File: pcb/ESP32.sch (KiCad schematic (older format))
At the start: 5 parts, among them U1 ESP32-WROOM

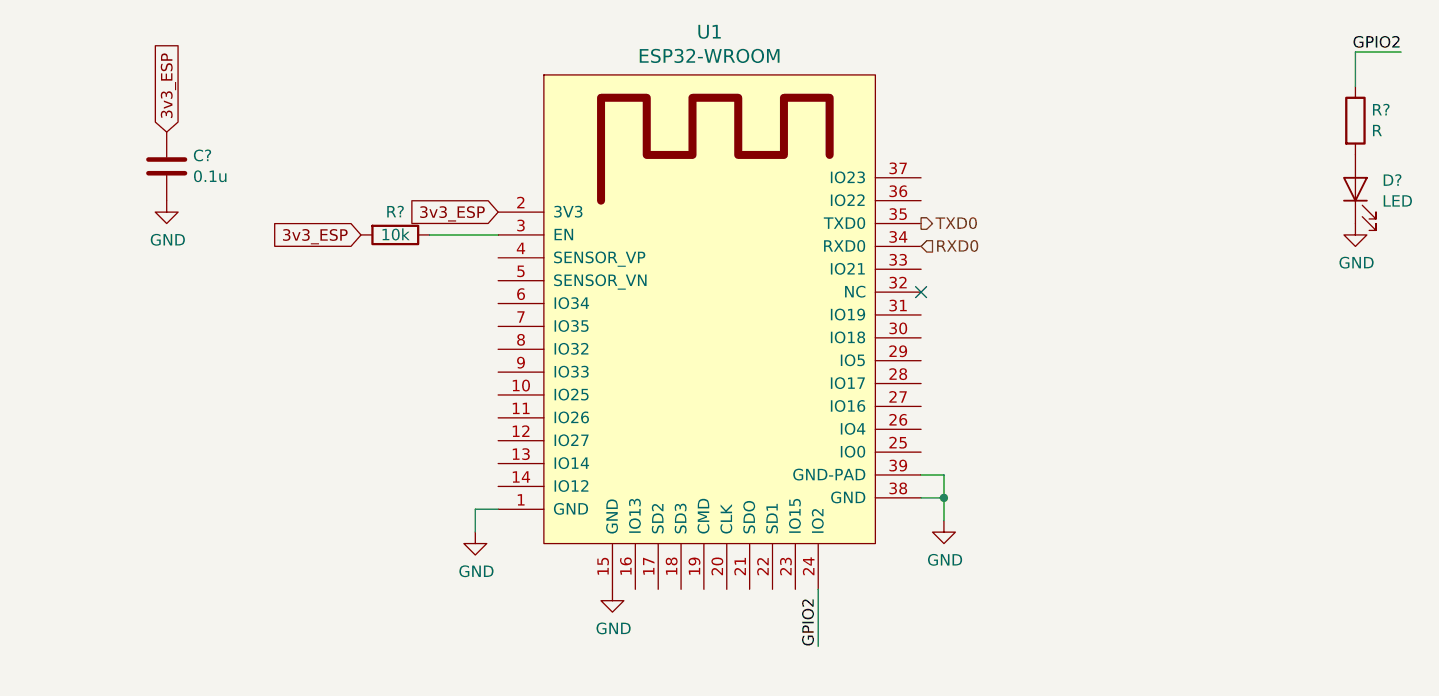
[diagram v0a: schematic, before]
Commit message: RTC to PCB
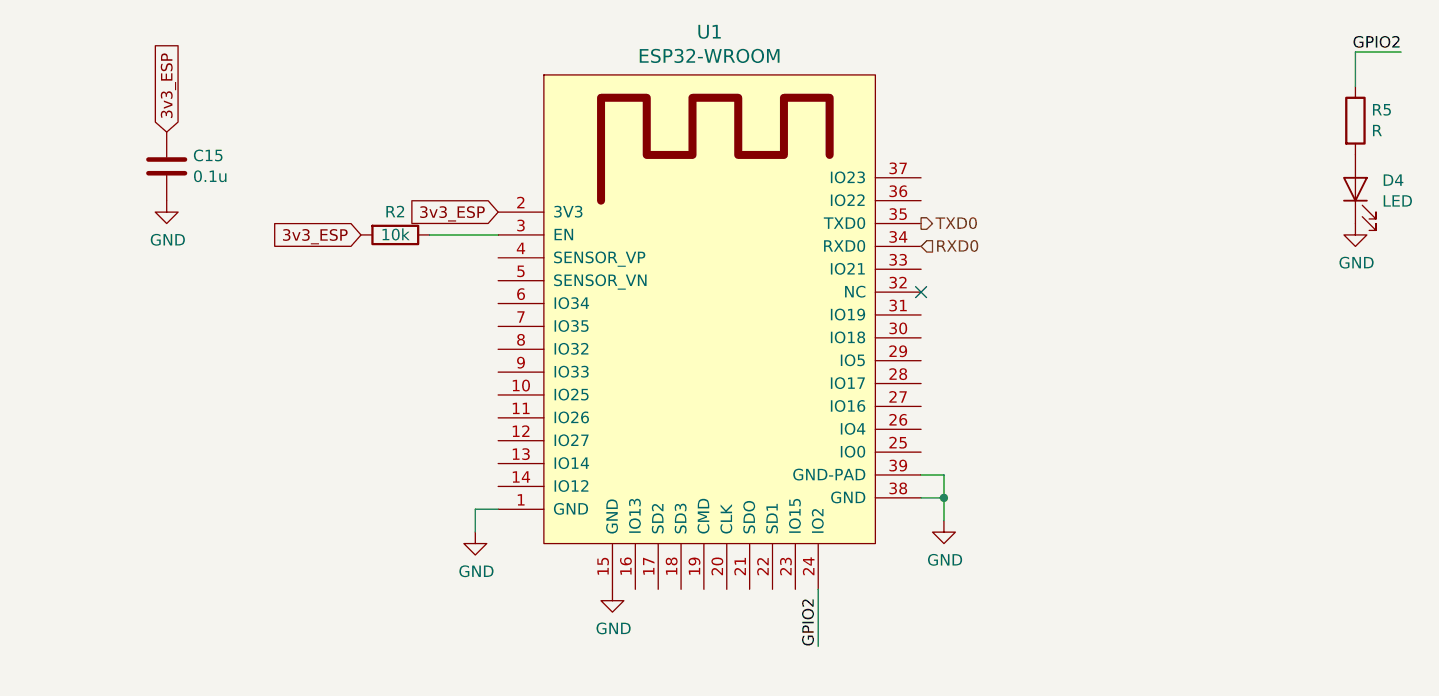
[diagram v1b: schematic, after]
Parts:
- gave numbers to parts that had none: 4
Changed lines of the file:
@@
 NoConn ~ 5150 2850
 $Comp
-L power:GND #PWR?
+L power:GND #PWR0101
 U 1 1 5E8F2039
 P 3800 4150
-F 0 "#PWR?" H 3800 3900 50  0001 C CNN
+F 0 "#PWR0101" H 3800 3900 50  0001 C CNN
 F 1 "GND" H 3805 3977 50  0000 C CNN
 F 2 "" H 3800 4150 50  0001 C CNN
@@
 $EndComp
 $Comp
-L power:GND #PWR?
+L power:GND #PWR0102
 U 1 1 5E8F205E
 P 3200 3900
-F 0 "#PWR?" H 3200 3650 50  0001 C CNN
+F 0 "#PWR0102" H 3200 3650 50  0001 C CNN
 F 1 "GND" H 3205 3727 50  0000 C CNN
 F 2 "" H 3200 3900 50  0001 C CNN
@@
 $EndComp
 $Comp
-L power:GND #PWR?
+L power:GND #PWR0103
 U 1 1 5E8F2083
 P 5250 3850
-F 0 "#PWR?" H 5250 3600 50  0001 C CNN
+F 0 "#PWR0103" H 5250 3600 50  0001 C CNN
 F 1 "GND" H 5255 3677 50  0000 C CNN
 F 2 "" H 5250 3850 50  0001 C CNN
@@
 3v3_ESP
 $Comp
-L Device:R R?
+L Device:R R2
 U 1 1 5E8F5CB8
 P 2850 2600
-F 0 "R?" V 2750 2600 50  0000 C CNN
+F 0 "R2" V 2750 2600 50  0000 C CNN
 F 1 "10k" V 2850 2600 50  0000 C CNN
 F 2 "" V 2780 2600 50  0001 C CNN
@@
 3v3_ESP
 $Comp
-L Device:C C?
+L Device:C C15
 U 1 1 5E8E7E17
 P 1850 2300
-F 0 "C?" H 1965 2346 50  0000 L CNN
+F 0 "C15" H 1965 2346 50  0000 L CNN
 F 1 "0.1u" H 1965 2255 50  0000 L CNN
 F 2 "" H 1888 2150 50  0001 C CNN
@@
 $EndComp
 $Comp
-L power:GND #PWR?
+L power:GND #PWR0104
 U 1 1 5E8E7EAA
 P 1850 2450
-F 0 "#PWR?" H 1850 2200 50  0001 C CNN
+F 0 "#PWR0104" H 1850 2200 50  0001 C CNN
 F 1 "GND" H 1855 2277 50  0000 C CNN
 F 2 "" H 1850 2450 50  0001 C CNN
@@
 $EndComp
 $Comp
-L Device:R R?
+L Device:R R5
 U 1 1 5E90464A
 P 7050 2100
-F 0 "R?" H 7120 2146 50  0000 L CNN
+F 0 "R5" H 7120 2146 50  0000 L CNN
 F 1 "R" H 7120 2055 50  0000 L CNN
 F 2 "" V 6980 2100 50  0001 C CNN
@@
 $EndComp
 $Comp
-L Device:LED D?
+L Device:LED D4
 U 1 1 5E9046C5
 P 7050 2400
-F 0 "D?" V 7088 2283 50  0000 R CNN
+F 0 "D4" V 7088 2283 50  0000 R CNN
 F 1 "LED" V 6997 2283 50  0000 R CNN
 F 2 "" H 7050 2400 50  0001 C CNN
@@
 $EndComp
 $Comp
-L power:GND #PWR?
+L power:GND #PWR0105
 U 1 1 5E904748
 P 7050 2550
-F 0 "#PWR?" H 7050 2300 50  0001 C CNN
+F 0 "#PWR0105" H 7050 2300 50  0001 C CNN
 F 1 "GND" H 7055 2377 50  0000 C CNN
 F 2 "" H 7050 2550 50  0001 C CNN

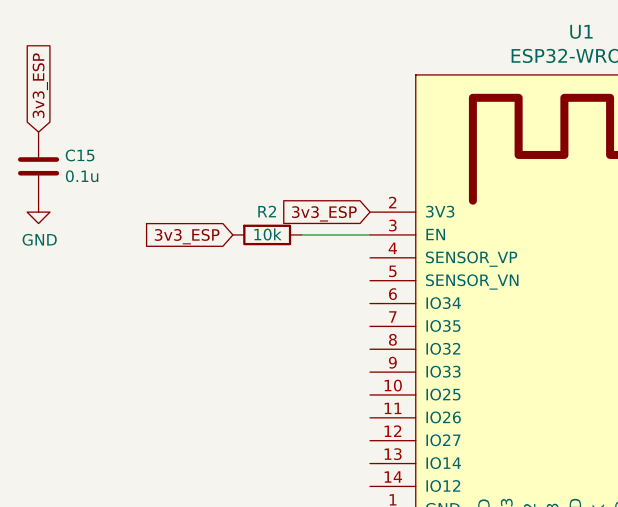
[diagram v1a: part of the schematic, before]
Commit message: added miscellaneous to electro valves sheet
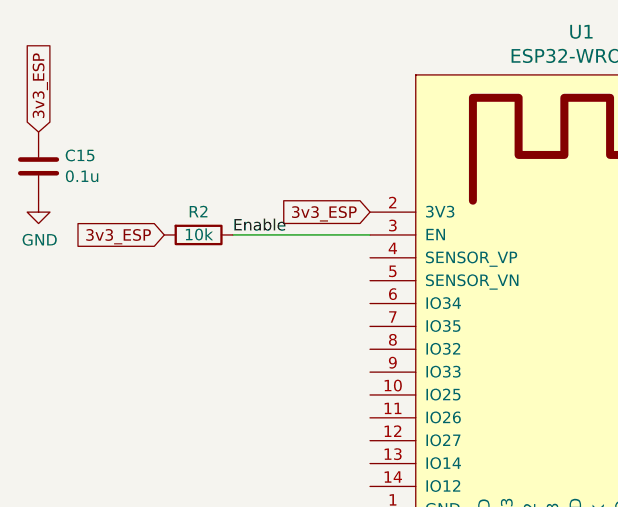
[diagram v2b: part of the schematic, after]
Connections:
- net Enable: now reaches R2.1, U1.3 (EN)
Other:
- moved on the sheet: R2
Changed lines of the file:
@@
 EESchema Schematic File Version 4
 LIBS:keep_breathing_ctrl-cache
-EELAYER 30 0
+EELAYER 26 0
 EELAYER END
 $Descr A4 11693 8268
@@
 L Device:R R2
 U 1 1 5E8F5CB8
-P 2850 2600
-F 0 "R2" V 2750 2600 50  0000 C CNN
-F 1 "10k" V 2850 2600 50  0000 C CNN
-F 2 "" V 2780 2600 50  0001 C CNN
-F 3 "~" H 2850 2600 50  0001 C CNN
-	1    2850 2600
+P 2550 2600
+F 0 "R2" V 2450 2600 50  0000 C CNN
+F 1 "10k" V 2550 2600 50  0000 C CNN
+F 2 "" V 2480 2600 50  0001 C CNN
+F 3 "~" H 2550 2600 50  0001 C CNN
+	1    2550 2600
 	0    1    1    0
 $EndComp
-Wire Wire Line
-	3000 2600 3300 2600
-Text GLabel 2700 2600 0    50   Input ~ 0
+Text GLabel 2400 2600 0    50   Input ~ 0
 3v3_ESP
 Text HLabel 5150 2550 2    50   Output ~ 0
@@
 Wire Wire Line
 	4700 4400 4700 4150
+Wire Wire Line
+	2700 2600 3300 2600
+Text Label 2700 2600 0    50   ~ 0
+Enable
 $EndSCHEMATC

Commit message: connecting esp32 signals
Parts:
- removed R2: 10k, symbol Device:R
- added C31: 10uF, Capacitor_SMD:C_0603_1608Metric, symbol Device:C_Small
- added C32: 10nF, Capacitor_SMD:C_0402_1005Metric, symbol Device:C_Small
- added R2, R30: 4.7k, Resistor_SMD:R_0402_1005Metric, symbol Device:R_Small
- C15: value 0.1u -> 0.1uF; footprint (none) -> Capacitor_SMD:C_0402_1005Metric; symbol Device:C -> Device:C_Small
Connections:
- net GND: now also C31.2, C32.2
- net IO25: now reaches U1.10 (IO25)
- net IO26: now reaches U1.11 (IO26)
- net IO27: now reaches U1.12 (IO27)
- net IO14: now reaches U1.13 (IO14)
- net IO12: now reaches U1.14 (IO12)
- net IO13: now reaches U1.16 (IO13)
- net PROG_EN: now reaches U1.25 (IO0)
- net PROG_EN: now also R30.2
- net IO4: now reaches U1.26 (IO4)
- net IO16: now reaches U1.27 (IO16)
- net IO17: now reaches U1.28 (IO17)
- net IO5: now reaches U1.29 (IO5)
- net IO18: now reaches U1.30 (IO18)
- net IO19: now reaches U1.31 (IO19)
- net IO21: now reaches U1.33 (IO21)
- net IO22: now reaches U1.36 (IO22)
- net IO23: now reaches U1.37 (IO23)
- net IO34: now reaches U1.6 (IO34)
- net IO35: now reaches U1.7 (IO35)
- net IO32: now reaches U1.8 (IO32)
- net IO33: now reaches U1.9 (IO33)
- net 3v3_ESP renamed 3V3_ESP
- net 3V3_ESP: now also C31.1, R2.1, R30.1
- net Enable renamed EN
- net EN: now also C32.1, R2.2
- no-connect marks 1 -> 10
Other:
- moved on the sheet: C15

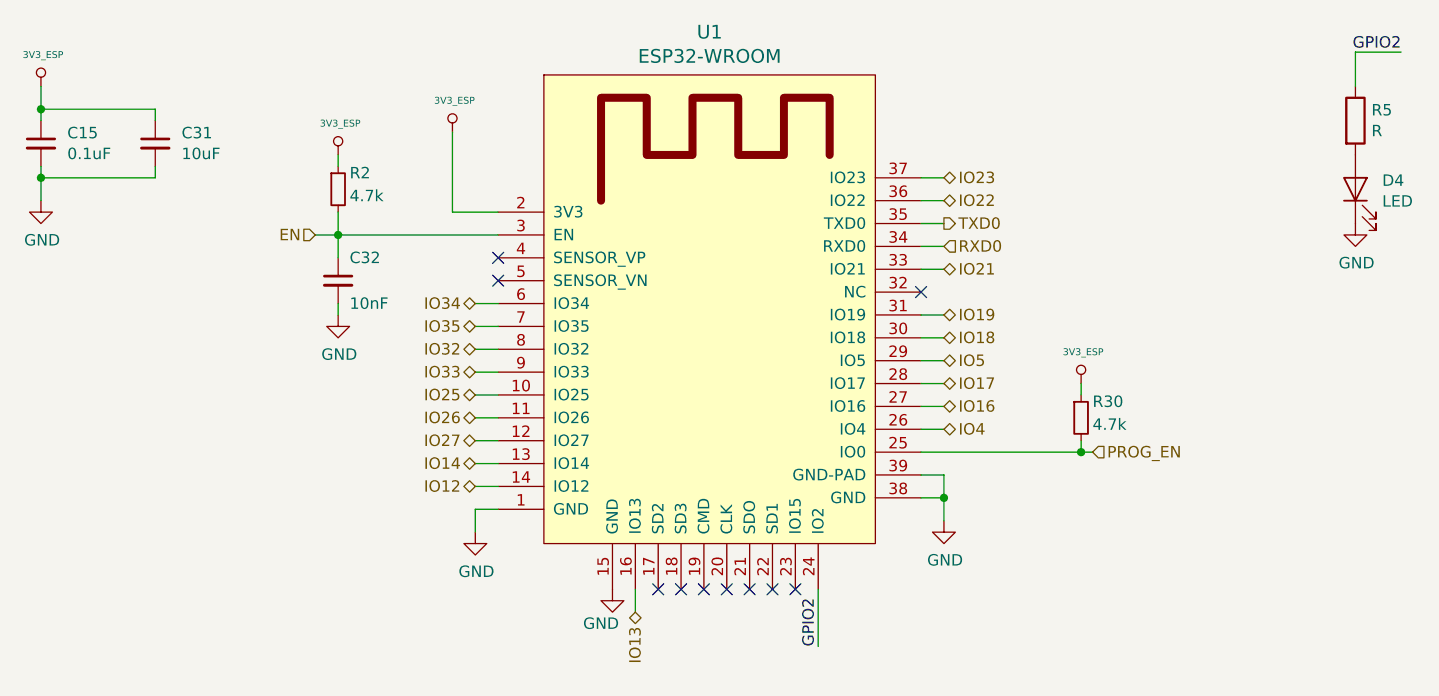
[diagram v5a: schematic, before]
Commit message: Connections in the schema were modified and components some components from supply and electrovalves were positioned on the PCB
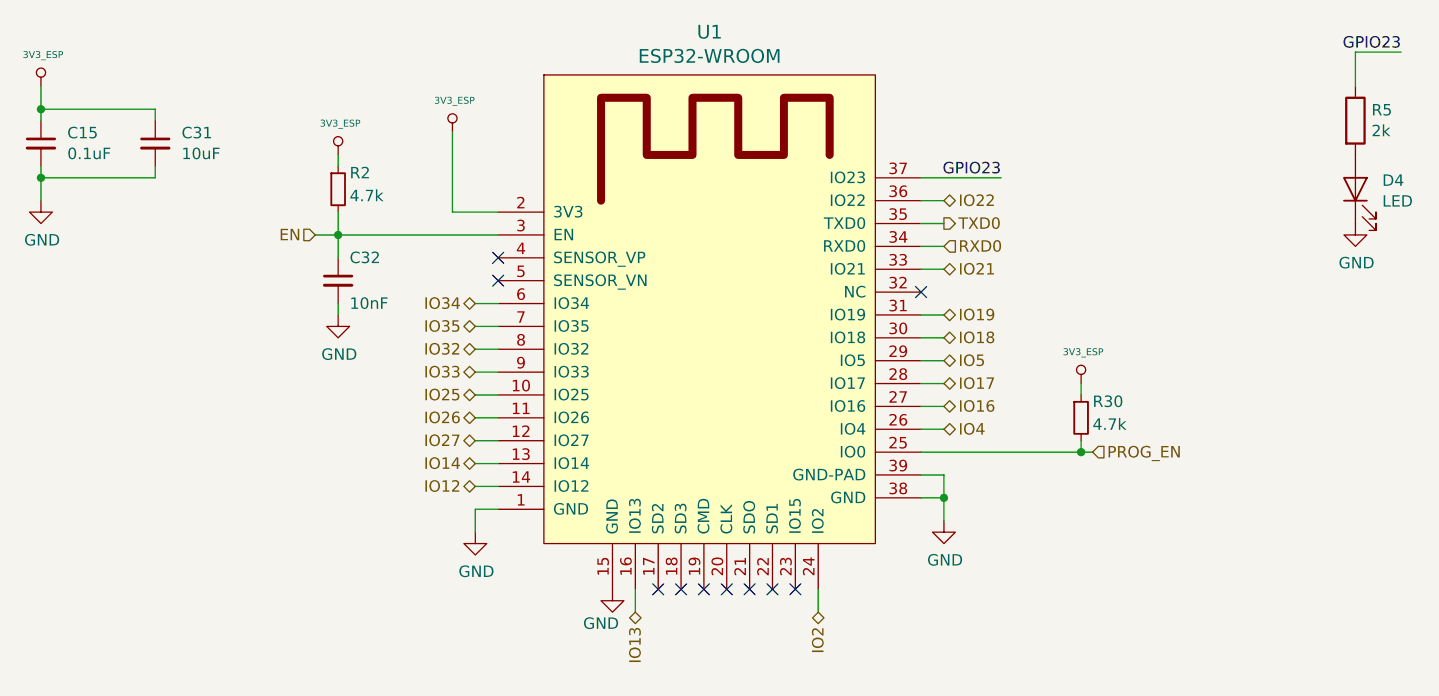
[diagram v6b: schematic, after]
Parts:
- D4: footprint (none) -> LED_SMD:LED_0805_2012Metric
- R5: value R -> 2k; footprint (none) -> Resistor_SMD:R_0402_1005Metric
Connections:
- net IO23 is gone; now on net GPIO23: U1.37 (IO23)
- net GPIO2 renamed GPIO23
- net GPIO23: no longer U1.24 (IO2)
- new net IO2: U1.24 (IO2)
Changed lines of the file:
@@
 P 7050 2100
 F 0 "R5" H 7120 2146 50  0000 L CNN
-F 1 "R" H 7120 2055 50  0000 L CNN
-F 2 "" V 6980 2100 50  0001 C CNN
+F 1 "2k" H 7120 2055 50  0000 L CNN
+F 2 "Resistor_SMD:R_0402_1005Metric" V 6980 2100 50  0001 C CNN
 F 3 "~" H 7050 2100 50  0001 C CNN
 	1    7050 2100
@@
 F 0 "D4" V 7088 2283 50  0000 R CNN
 F 1 "LED" V 6997 2283 50  0000 R CNN
-F 2 "" H 7050 2400 50  0001 C CNN
+F 2 "LED_SMD:LED_0805_2012Metric" H 7050 2400 50  0001 C CNN
 F 3 "~" H 7050 2400 50  0001 C CNN
 	1    7050 2400
@@
 $EndComp
 Text Label 7250 1800 2    50   ~ 0
-GPIO2
+GPIO23
 Wire Wire Line
 	7050 1800 7250 1800
 Wire Wire Line
 	7050 1800 7050 1950
-Text Label 4700 4400 1    50   ~ 0
-GPIO2
-Wire Wire Line
-	4700 4400 4700 4150
+Text Label 5500 2350 2    50   ~ 0
+GPIO23
 $Comp
 L ventilator-PowerSymbols:3V3_ESP #PWR0160
@@
 Text HLabel 5900 3550 2    50   Input ~ 0
 PROG_EN
-Text HLabel 5250 2350 2    50   BiDi ~ 0
-IO23
+Text HLabel 4700 4250 3    50   BiDi ~ 0
+IO2
 Text HLabel 5250 2450 2    50   BiDi ~ 0
 IO22
-Wire Wire Line
-	5150 2350 5250 2350
 Wire Wire Line
 	5150 2450 5250 2450
@@
 Wire Wire Line
 	2600 2700 2600 2600
+Wire Wire Line
+	5150 2350 5500 2350
+Wire Wire Line
+	4700 4250 4700 4150
 $EndSCHEMATC
